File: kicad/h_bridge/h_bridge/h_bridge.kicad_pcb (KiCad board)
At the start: 2 copper layers, 56 parts, among them J1 Conn_01x04_Male, J2 voltage_in, J3 motor, Q1 IRF3205, Q2 IRF3205, Q3 IRF3205, Q4 IRF3205, Q5 IRF3205, Q6 IRF3205, Q7 IRF3205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

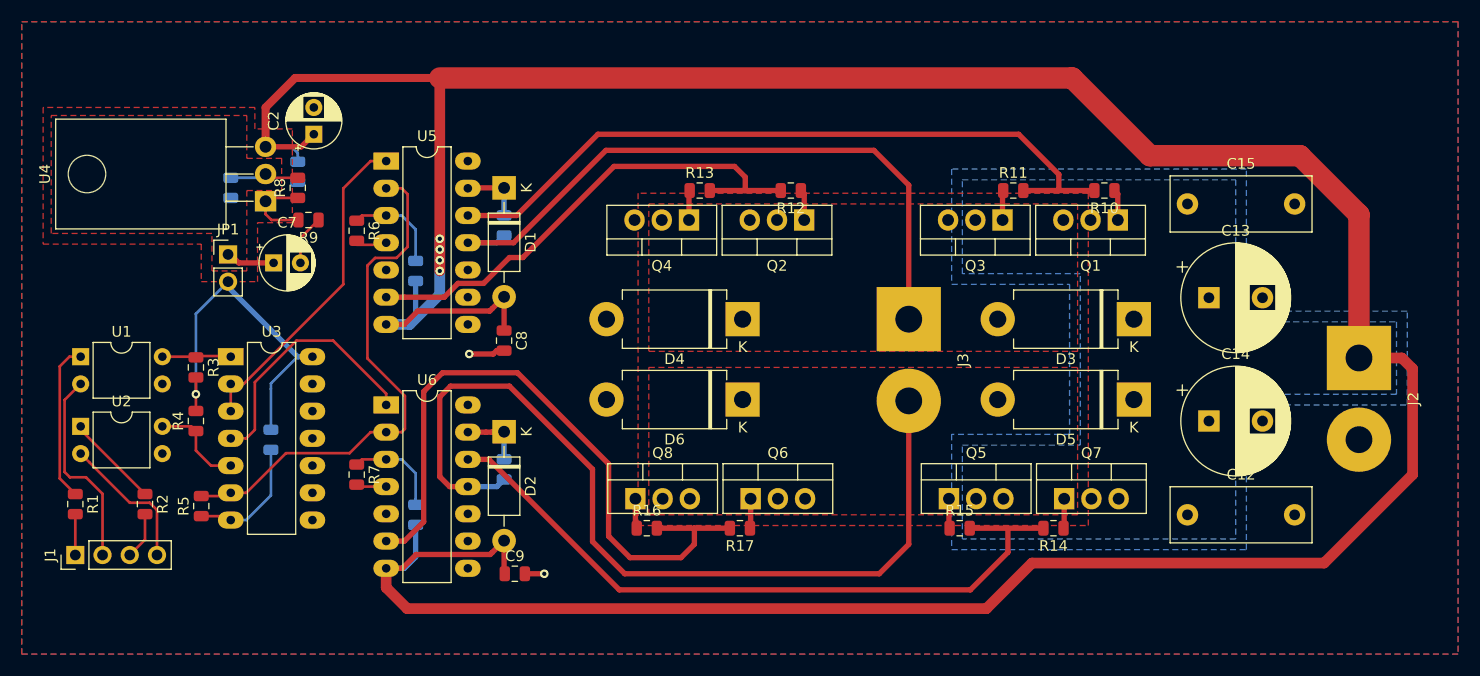
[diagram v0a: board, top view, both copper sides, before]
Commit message: [kicad/h_bridge] layout improvements; also added gerber
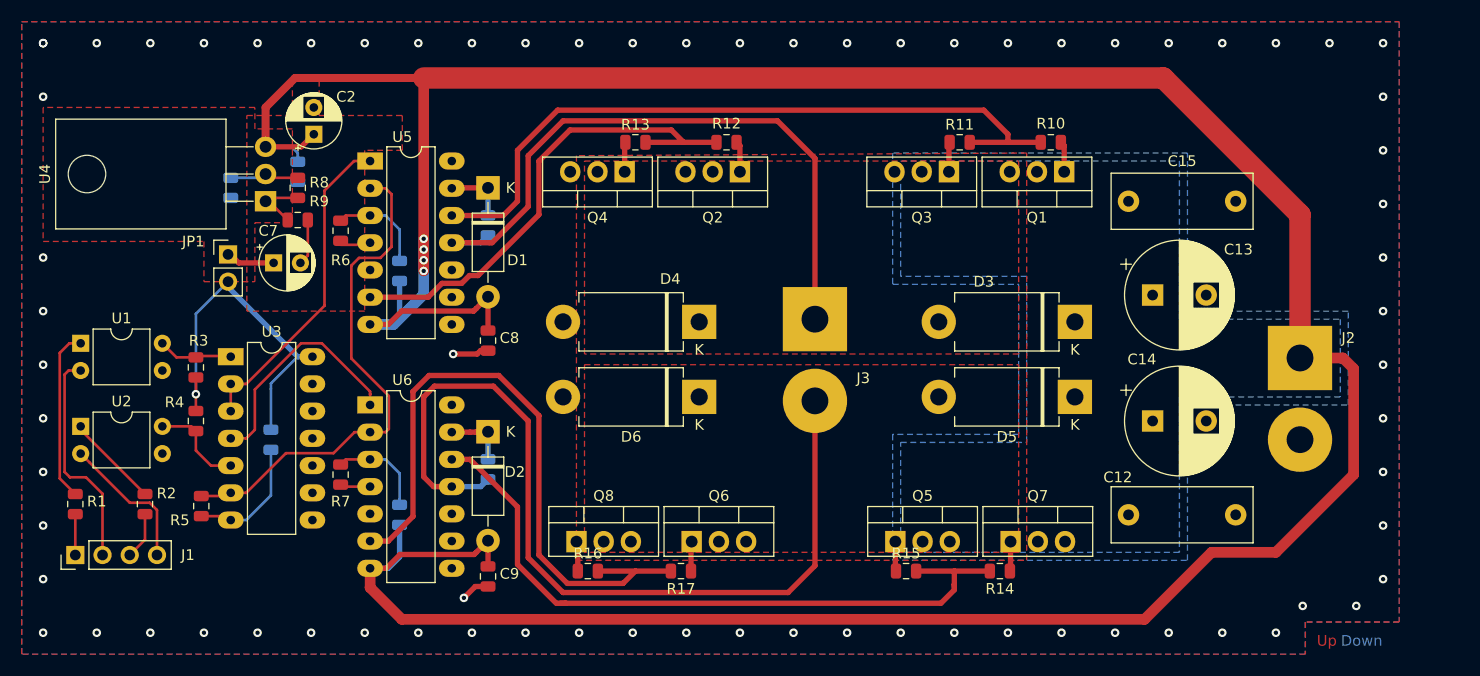
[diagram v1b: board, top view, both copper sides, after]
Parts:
- moved J3 8.75 mm to (174.5, 125.8)
- moved Q2 7.50 mm to (167.5, 112.0)
- moved Q4 7.50 mm to (156.8, 112.0)
- moved R12 7.50 mm to (166.2, 109.2)
- moved R13 7.50 mm to (157.8, 109.2)
- moved Q6 6.80 mm to (163.0, 146.5)
- moved Q8 6.80 mm to (152.2, 146.5)
- moved R16 6.80 mm to (153.3, 149.2)
- moved R17 6.80 mm to (162.0, 149.2)
- moved Q1 6.73 mm to (197.8, 112.0)
- moved Q3 6.73 mm to (187.0, 112.0)
- moved R10 6.73 mm to (196.5, 109.2)
- moved R11 6.73 mm to (188.0, 109.2)
- moved Q5 6.40 mm to (182.0, 146.5)
- moved Q7 6.40 mm to (192.8, 146.5)
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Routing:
- net VCC: track 322.6 -> 313.2 mm
- net /pwm_right: track 24.0 -> 22.0 mm
- net Net-(J1-Pad2): track 18.9 -> 20.8 mm
- net Net-(R8-Pad1): track 7.62 -> 5.92 mm
- net /!enable: track 49.9 -> 48.4 mm
- net /right_low: track 62.3 -> 60.9 mm
- net /left_low: track 47.1 -> 45.7 mm
- net Net-(R1-Pad1): track 14.8 -> 16.1 mm
- net /right_motor: track 84.2 -> 83.1 mm
- net /left_high: track 67.9 -> 67.0 mm
- net /pwm_left: track 30.9 -> 31.7 mm
- net Net-(R3-Pad1): track 6.43 -> 7.16 mm
- net /left_motor: track 62.2 -> 61.5 mm
- net GND: track 40.6 -> 41.1 mm, vias 2 -> 73
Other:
- board text added: "Down"
- board text added: "Up"

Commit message: [kicad/h_bridge] layout done I think
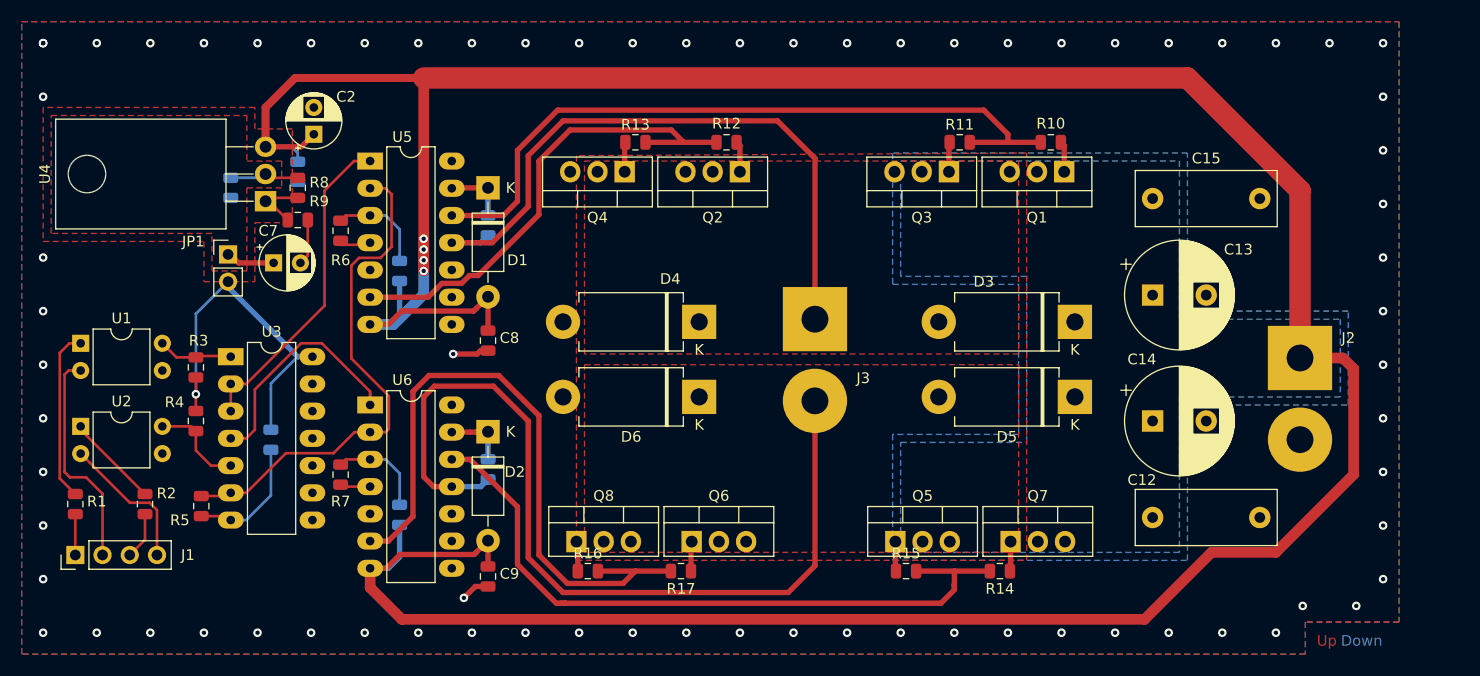
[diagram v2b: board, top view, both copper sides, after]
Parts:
- moved C12 2.26 mm to (206.0, 144.2)
- moved C15 2.26 mm to (206.0, 114.5)
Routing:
- net VCC: track 313.2 -> 314.5 mm
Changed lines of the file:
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@@
   )
   (module Capacitor_THT:C_Rect_L13.0mm_W5.0mm_P10.00mm_FKS3_FKP3_MKS4 (layer F.Cu)
-    (at 203.75 144)
+    (at 206 144.25)
     (descr "C, Rect series, Radial, pin pitch=10.00mm, , length*width=13*5mm^2, Capacitor, http://www.wima.com/EN/WIMA_FKS_3.pdf, http://www.wima.com/EN/WIMA_MKS_4.pdf")
     (tags "C Rect series Radial pin pitch 10.00mm  length 13mm width 5mm Capacitor")
@@
   )
   (module Capacitor_THT:C_Rect_L13.0mm_W5.0mm_P10.00mm_FKS3_FKP3_MKS4 (layer F.Cu)
-    (at 203.75 114.75)
+    (at 206 114.5)
     (descr "C, Rect series, Radial, pin pitch=10.00mm, , length*width=13*5mm^2, Capacitor, http://www.wima.com/EN/WIMA_FKS_3.pdf, http://www.wima.com/EN/WIMA_MKS_4.pdf")
     (tags "C Rect series Radial pin pitch 10.00mm  length 13mm width 5mm Capacitor")
@@
   (segment (start 224.75 140.25) (end 217.5 147.5) (width 1) (layer F.Cu) (net 3))
   (segment (start 217.5 147.5) (end 211.5 147.5) (width 1) (layer F.Cu) (net 3))
-  (segment (start 219.75 129.37) (end 219.75 116) (width 2) (layer F.Cu) (net 3))
-  (segment (start 219.75 116) (end 207 103.25) (width 2) (layer F.Cu) (net 3))
   (segment (start 126 103.25) (end 138 103.25) (width 0.75) (layer F.Cu) (net 3))
   (segment (start 144 148.8125) (end 144 146.41) (width 0.5) (layer F.Cu) (net 3))
   (segment (start 211.5 147.5) (end 205.25 153.75) (width 1) (layer F.Cu) (net 3))
   (segment (start 205.25 153.75) (end 135.96 153.75) (width 1) (layer F.Cu) (net 3))
-  (segment (start 207 103.25) (end 138 103.25) (width 2) (layer F.Cu) (net 3))
+  (segment (start 209.25 103.25) (end 138 103.25) (width 2) (layer F.Cu) (net 3))
+  (segment (start 219.75 129.37) (end 219.75 113.75) (width 2) (layer F.Cu) (net 3))
+  (segment (start 219.75 113.75) (end 209.25 103.25) (width 2) (layer F.Cu) (net 3))
   (segment (start 120.75 120.5) (end 119.75 119.5) (width 0.5) (layer F.Cu) (net 4) (status 20))
   (segment (start 122.8975 112.5625) (end 123.25 112.21) (width 0.25) (layer B.Cu) (net 4))
@@
     (connect_pads yes (clearance 0.254))
     (min_thickness 0.254)
-    (fill (arc_segments 32) (thermal_gap 0.254) (thermal_bridge_width 0.508) (smoothing fillet) (radius 0.5))
+    (fill yes (arc_segments 32) (thermal_gap 0.254) (thermal_bridge_width 0.508) (smoothing fillet) (radius 0.5))
     (polygon
       (pts
@@
     (connect_pads yes (clearance 0.254))
     (min_thickness 0.254)
-    (fill (arc_segments 32) (thermal_gap 0.254) (thermal_bridge_width 0.508) (smoothing fillet) (radius 0.5))
+    (fill yes (arc_segments 32) (thermal_gap 0.254) (thermal_bridge_width 0.508) (smoothing fillet) (radius 0.5))
     (polygon
       (pts
@@
     (connect_pads yes (clearance 0.254))
     (min_thickness 0.254)
-    (fill (arc_segments 32) (thermal_gap 0.254) (thermal_bridge_width 0.508) (smoothing fillet) (radius 0.5))
+    (fill yes (arc_segments 32) (thermal_gap 0.254) (thermal_bridge_width 0.508) (smoothing fillet) (radius 0.5))
     (polygon
       (pts
@@
     (connect_pads yes (clearance 0.254))
     (min_thickness 0.254)
-    (fill (arc_segments 32) (thermal_gap 0.254) (thermal_bridge_width 0.508) (smoothing fillet) (radius 0.5))
+    (fill yes (arc_segments 32) (thermal_gap 0.254) (thermal_bridge_width 0.508) (smoothing fillet) (radius 0.5))
     (polygon
       (pts
-        (xy 121.5 106.75) (xy 125.75 106.75) (xy 125.75 103.5) (xy 128.25 103.5) (xy 128.25 106.75)
-        (xy 136 106.75) (xy 136 110) (xy 132.5 110) (xy 132.5 125) (xy 121.5 125)
+        (xy 121.5 106.75) (xy 121.5 111) (xy 124.75 111) (xy 124.75 113.5) (xy 121.5 113.5)
+        (xy 121.5 121.25) (xy 118.25 121.25) (xy 118.25 117.75) (xy 103.25 117.75) (xy 103.25 106.75)
       )
     )
@@
     (connect_pads yes (clearance 0.508))
     (min_thickness 0.254)
-    (fill (arc_segments 32) (thermal_gap 0.508) (thermal_bridge_width 0.508))
+    (fill yes (arc_segments 32) (thermal_gap 0.508) (thermal_bridge_width 0.508))
     (polygon
       (pts
@@
     (connect_pads (clearance 0.508))
     (min_thickness 0.254)
-    (fill (arc_segments 32) (thermal_gap 0.508) (thermal_bridge_width 0.508) (smoothing fillet) (radius 0.5))
+    (fill yes (arc_segments 32) (thermal_gap 0.508) (thermal_bridge_width 0.508) (smoothing fillet) (radius 0.5))
     (polygon
       (pts
@@
     (connect_pads (clearance 0.508))
     (min_thickness 0.254)
-    (fill (arc_segments 32) (thermal_gap 0.508) (thermal_bridge_width 0.508) (smoothing fillet) (radius 0.5))
+    (fill yes (arc_segments 32) (thermal_gap 0.508) (thermal_bridge_width 0.508) (smoothing fillet) (radius 0.5))
     (polygon
       (pts

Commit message: [kicad/h_bridge] small changes
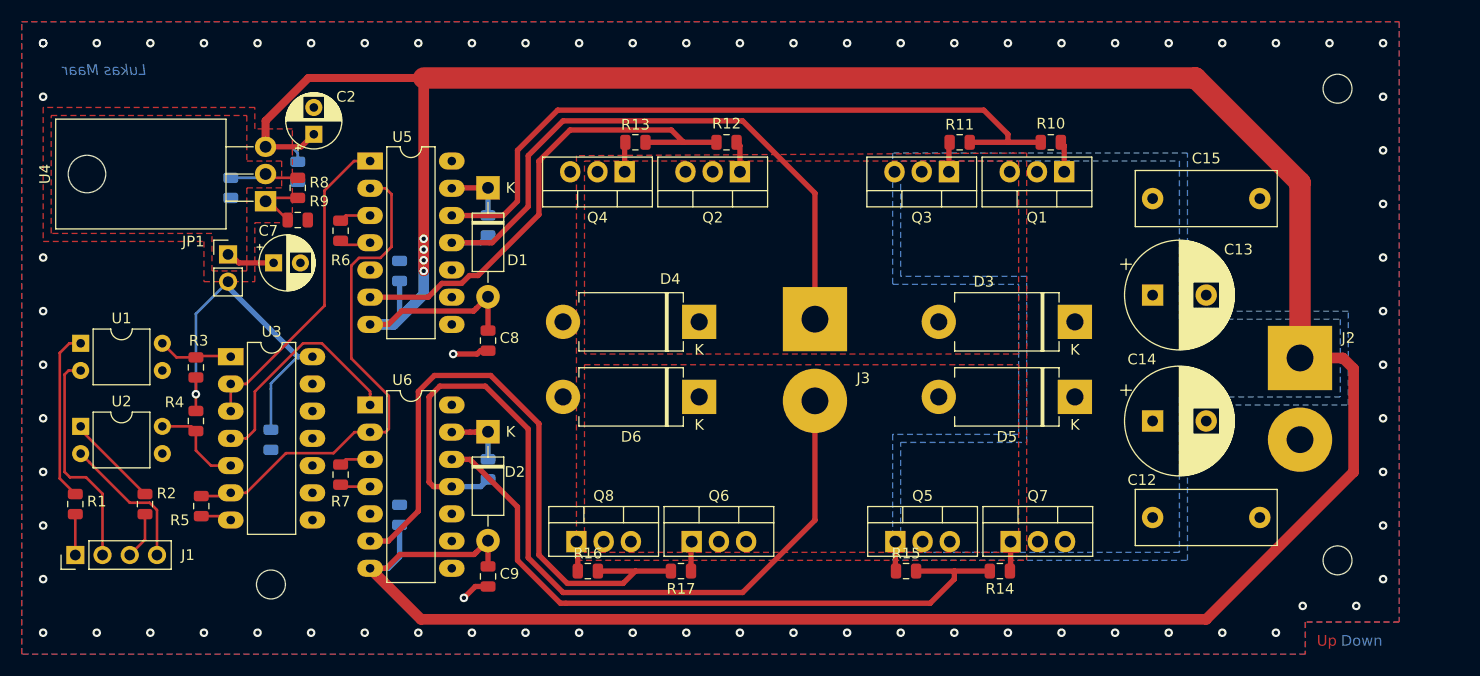
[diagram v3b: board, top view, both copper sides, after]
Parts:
- added REF**: MountingHole_2.7mm, MountingHole:MountingHole_2.7mm, F.Cu at (123.8, 150.5)
- added REF**: MountingHole_2.7mm, MountingHole:MountingHole_2.7mm, F.Cu at (223.2, 148.2)
- added REF**: MountingHole_2.7mm, MountingHole:MountingHole_2.7mm, F.Cu at (223.2, 104.2)
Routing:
- net GND: track 41.1 -> 15.4 mm
- net /right_motor: track 83.1 -> 79.4 mm
- net /left_motor: track 61.5 -> 59.6 mm
- net /right_high: track 66.2 -> 64.6 mm
- net VCC: track 314.5 -> 313.0 mm
- net /right_low: track 60.9 -> 60.2 mm
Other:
- board text added: "Lukas Maar"

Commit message: [kicad/h_bridge] small changes
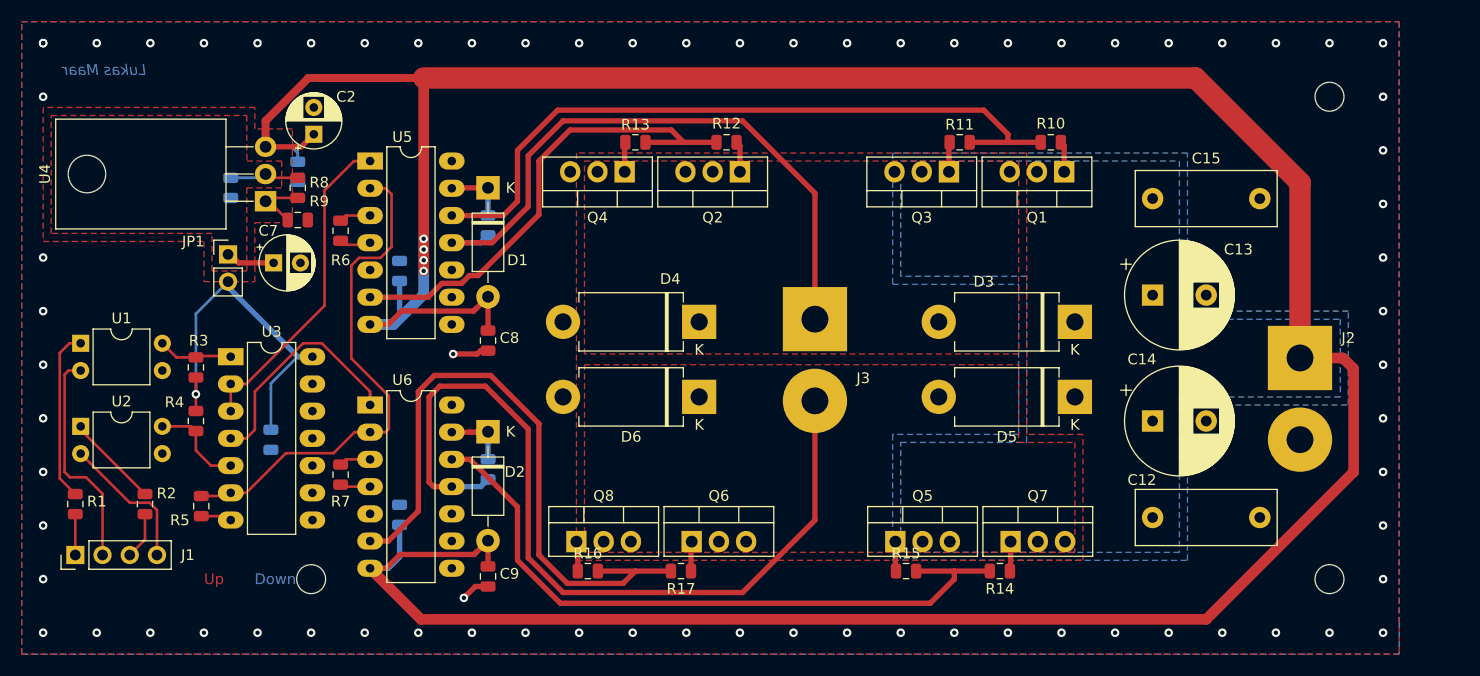
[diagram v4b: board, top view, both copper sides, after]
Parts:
- removed the REF** at (123.8, 150.5)
- removed the REF** at (223.2, 148.2)
- added REF**: MountingHole_2.7mm, MountingHole:MountingHole_2.7mm, F.Cu at (127.5, 150.0)
- added REF**: MountingHole_2.7mm, MountingHole:MountingHole_2.7mm, F.Cu at (222.5, 150.0)
- moved REF** 1.06 mm to (222.5, 105.0)
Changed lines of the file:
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@@
   )
   (module MountingHole:MountingHole_2.7mm (layer F.Cu)
-    (at 123.75 150.5)
+    (at 127.5 150)
     (descr "Mounting Hole 2.7mm, no annular")
     (tags "mounting hole 2.7mm no annular")
@@
   )
   (module MountingHole:MountingHole_2.7mm (layer F.Cu)
-    (at 223.25 148.25)
+    (at 222.5 150)
     (descr "Mounting Hole 2.7mm, no annular")
     (tags "mounting hole 2.7mm no annular")
@@
   )
   (module MountingHole:MountingHole_2.7mm (layer F.Cu)
-    (at 223.25 104.25)
+    (at 222.5 105)
     (descr "Mounting Hole 2.7mm, no annular")
     (tags "mounting hole 2.7mm no annular")
@@
     (effects (font (size 1 1) (thickness 0.15) italic) (justify mirror))
   )
-  (gr_text Down (at 225.5 155.75) (layer B.Cu)
-    (effects (font (size 1 1) (thickness 0.2)))
+  (gr_text "   Down   " (at 126.1 150) (layer B.Cu)
+    (effects (font (size 1 1) (thickness 0.2)) (justify right))
   )
-  (gr_text Up (at 222.25 155.75) (layer F.Cu)
-    (effects (font (size 1 1) (thickness 0.2)))
+  (gr_text "Up         " (at 117.5 150) (layer F.Cu)
+    (effects (font (size 1 1) (thickness 0.2)) (justify left))
   )
   (via (at 102.5 100) (size 0.8) (drill 0.4) (layers F.Cu B.Cu) (net 1))
@@
   (via (at 217.5 155) (size 0.8) (drill 0.4) (layers F.Cu B.Cu) (net 1))
   (via (at 202.5 155) (size 0.8) (drill 0.4) (layers F.Cu B.Cu) (net 1))
-  (via (at 220 152.5) (size 0.8) (drill 0.4) (layers F.Cu B.Cu) (net 1))
+  (via (at 222.5 155) (size 0.8) (drill 0.4) (layers F.Cu B.Cu) (net 1))
   (via (at 187.5 155) (size 0.8) (drill 0.4) (layers F.Cu B.Cu) (net 1))
   (via (at 172.5 155) (size 0.8) (drill 0.4) (layers F.Cu B.Cu) (net 1))
@@
   (via (at 182.5 100) (size 0.8) (drill 0.4) (layers F.Cu B.Cu) (net 1))
   (via (at 122.5 100) (size 0.8) (drill 0.4) (layers F.Cu B.Cu) (net 1))
-  (via (at 225 152.5) (size 0.8) (drill 0.4) (layers F.Cu B.Cu) (net 1))
+  (via (at 227.5 155) (size 0.8) (drill 0.4) (layers F.Cu B.Cu) (net 1))
   (via (at 227.5 105) (size 0.8) (drill 0.4) (layers F.Cu B.Cu) (net 1))
   (via (at 227.5 125) (size 0.8) (drill 0.4) (layers F.Cu B.Cu) (net 1))
@@
   (segment (start 121.45 131.79) (end 120 131.79) (width 0.25) (layer F.Cu) (net 34))
   (segment (start 133 111) (end 131.5 111) (width 0.25) (layer F.Cu) (net 34))
-  (zone (net 5) (net_name /left_motor) (layer F.Cu) (hatch edge 0.508)
-    (connect_pads yes (clearance 0.254))
-    (min_thickness 0.254)
-    (fill yes (arc_segments 32) (thermal_gap 0.254) (thermal_bridge_width 0.508) (smoothing fillet) (radius 0.5))
-    (polygon
-      (pts
-        (xy 153 129) (xy 153 111) (xy 193.5 111) (xy 193.5 129)
-      )
-    )
-  )
-  (zone (net 7) (net_name /right_motor) (layer F.Cu) (hatch edge 0.508)
-    (connect_pads yes (clearance 0.254))
-    (min_thickness 0.254)
-    (fill yes (arc_segments 32) (thermal_gap 0.254) (thermal_bridge_width 0.508) (smoothing fillet) (radius 0.5))
-    (polygon
-      (pts
-        (xy 153 147.5) (xy 153 130) (xy 193.5 130) (xy 193.5 147.5)
-      )
-    )
-  )
   (zone (net 3) (net_name VCC) (layer B.Cu) (hatch edge 0.508)
     (connect_pads yes (clearance 0.254))
@@
     (polygon
       (pts
-        (xy 220.25 154) (xy 220.25 157) (xy 100.5 157) (xy 100.5 98) (xy 229 98)
+        (xy 229 157) (xy 220.25 157) (xy 100.5 157) (xy 100.5 98) (xy 229 98)
         (xy 229 154)
       )
@@
     )
   )
+  (zone (net 5) (net_name /left_motor) (layer F.Cu) (hatch edge 0.508)
+    (connect_pads yes (clearance 0.254))
+    (min_thickness 0.254)
+    (fill yes (arc_segments 32) (thermal_gap 0.254) (thermal_bridge_width 0.508) (smoothing fillet) (radius 0.5))
+    (polygon
+      (pts
+        (xy 153 129) (xy 153 111) (xy 193.5 111) (xy 193.5 129)
+      )
+    )
+  )
   (zone (net 1) (net_name GND) (layer F.Cu) (hatch edge 0.508)
     (connect_pads (clearance 0.508))
@@
     (polygon
       (pts
-        (xy 220.25 157) (xy 100.5 157) (xy 100.5 98) (xy 229 98) (xy 229 154)
-        (xy 220.25 154)
+        (xy 229 157) (xy 100.5 157) (xy 100.5 98) (xy 229 98)
       )
     )
     (polygon
       (pts
-        (xy 152.25 110.5) (xy 152.25 148.25) (xy 194.25 148.25) (xy 194.25 110.25)
+        (xy 152.25 110.25) (xy 152.25 148.25) (xy 199.5 148.25) (xy 199.5 136.5) (xy 194.25 136.5)
+        (xy 194.25 110.25)
       )
     )
@@
       )
     )
+  )
+  (zone (net 7) (net_name /right_motor) (layer F.Cu) (hatch edge 0.508)
+    (connect_pads yes (clearance 0.508))
+    (min_thickness 0.254)
+    (fill yes (arc_segments 32) (thermal_gap 0.508) (thermal_bridge_width 0.508) (smoothing fillet) (radius 0.5))
+    (polygon
+      (pts
+        (xy 193.5 137.25) (xy 198.75 137.25) (xy 198.75 147.5) (xy 153 147.5) (xy 153 130)
+        (xy 193.5 130)
+      )
+    )
